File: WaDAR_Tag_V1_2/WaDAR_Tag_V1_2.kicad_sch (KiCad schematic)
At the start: 11 parts, among them J1 SMA-J-P-H-RA-TH1, U1 SiT1569

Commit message: added footprint for SiT1549
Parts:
- U1: footprint (none) -> Library:SiT1569
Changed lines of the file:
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@@
 			)
 		)
-		(property "Footprint" ""
+		(property "Footprint" "Library:SiT1569"
 			(at 67.31 81.28 0)
 			(effects

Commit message: PCB
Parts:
- removed TP1: VCC, JLab_FP:EpicTestPointV1, symbol Connector:TestPoint
- removed TP2: GND, JLab_FP:EpicTestPointV1, symbol Connector:TestPoint
- removed TP3: CLK_OUT, JLab_FP:EpicTestPointV1, symbol Connector:TestPoint

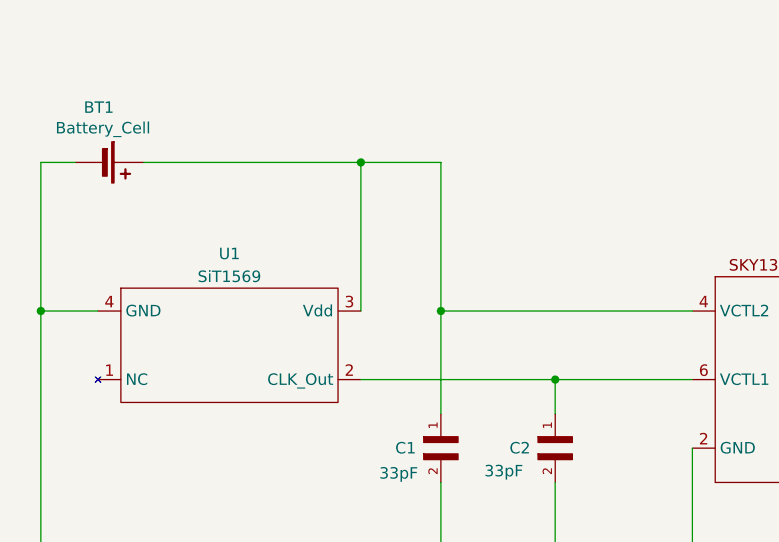
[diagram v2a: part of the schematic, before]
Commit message: added test points, made PCB double sided
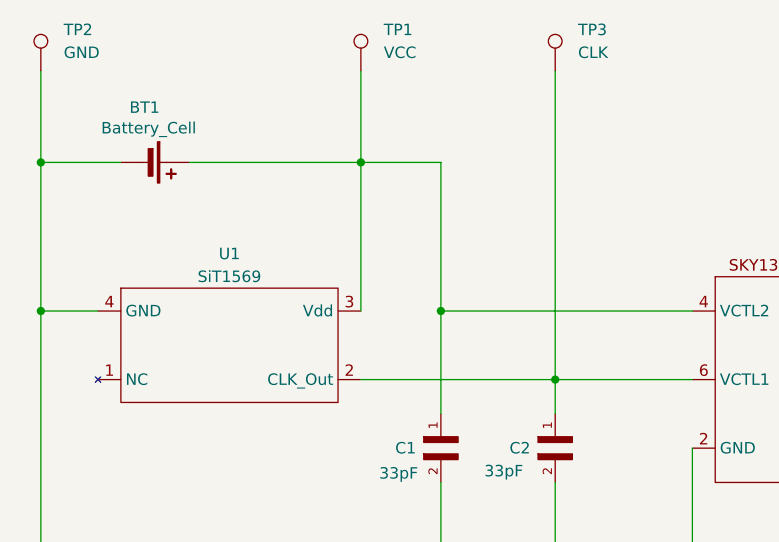
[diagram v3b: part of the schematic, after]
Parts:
- added TP1: VCC, TestPoint:TestPoint_Pad_D1.0mm, symbol Connector:TestPoint
- added TP2: GND, TestPoint:TestPoint_Pad_D1.0mm, symbol Connector:TestPoint
- added TP3: CLK, TestPoint:TestPoint_Pad_D1.0mm, symbol Connector:TestPoint
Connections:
- net GND: now also TP2.1
- net at BT1.1 (+), C1.1, U1.3 (Vdd)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: now also TP1.1
- net at C2.1, U1.2 (CLK_Out), U2.6 (VCTL1): now also TP3.1
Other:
- moved on the sheet: BT1

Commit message: updated datasheets
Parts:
- BT1: value Battery_Cell -> 1060
- C1, C2, C4: symbol GJM1555C1H330JB01D:GJM1555C1H330JB01D -> Device:C
- C3: symbol CBR04C101J3GAC:CBR04C101J3GAC -> Device:C
- U1: value SiT1569 -> SIT1569AC-J3-30E-0000.080000
- U2: value ~ -> SKY13351-378LF; footprint JLab_FP:SKY13351_FP -> Library:SKY13351_FP

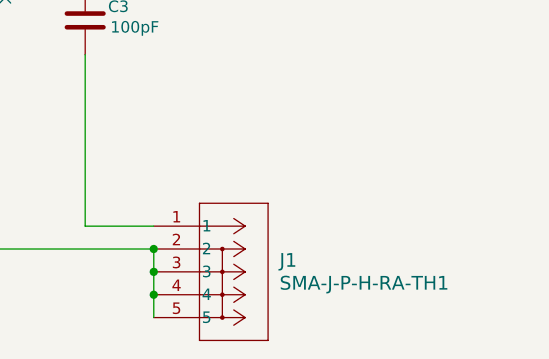
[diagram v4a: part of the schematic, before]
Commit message: added new RF junction
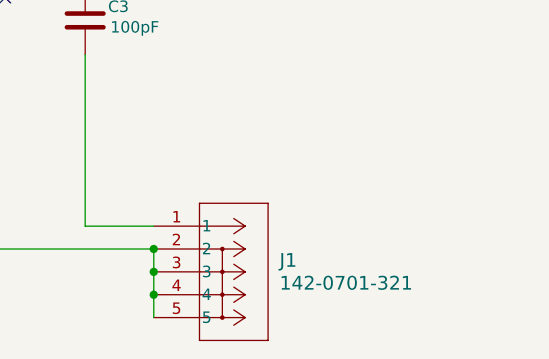
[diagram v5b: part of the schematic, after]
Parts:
- J1: value SMA-J-P-H-RA-TH1 -> 142-0701-321
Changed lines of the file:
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@@
 			)
 		)
-		(property "Value" "SMA-J-P-H-RA-TH1"
+		(property "Value" "142-0701-321"
 			(at 172.72 116.84 0)
 			(effects
@@
 			)
 		)
-		(property "Datasheet" "SMA-J-P-H-RA-TH1"
+		(property "Datasheet" "https://secure-web.cisco.com/1DZ9VzbYAXZ-R-LPek44dWAY5tpyuDxEmXSDugOLt9HCVcz2LxcBg_oyr93yuw77llLCRc9d3T34vo-pjBK-s3IkY3R66W-ncmQ0YOM9IQMUK1O7wZMPkewxqXqTqhK5-2u-29hxEuVjo2LqNmdOEcCusiwmr3znwXKvoiuOikGmvCtdp23G3hZo508RFRhTmv9uOTL0b0hJ-cT9kvkwjuFS8DTf5pSmEP"
 			(at 158.75 110.49 0)
 			(effects
@@
 			)
 		)
-		(property "Description" ""
+		(property "Description" "CONN SMA JACK R/A 50 OHM PCB"
 			(at 158.75 110.49 0)
 			(effects

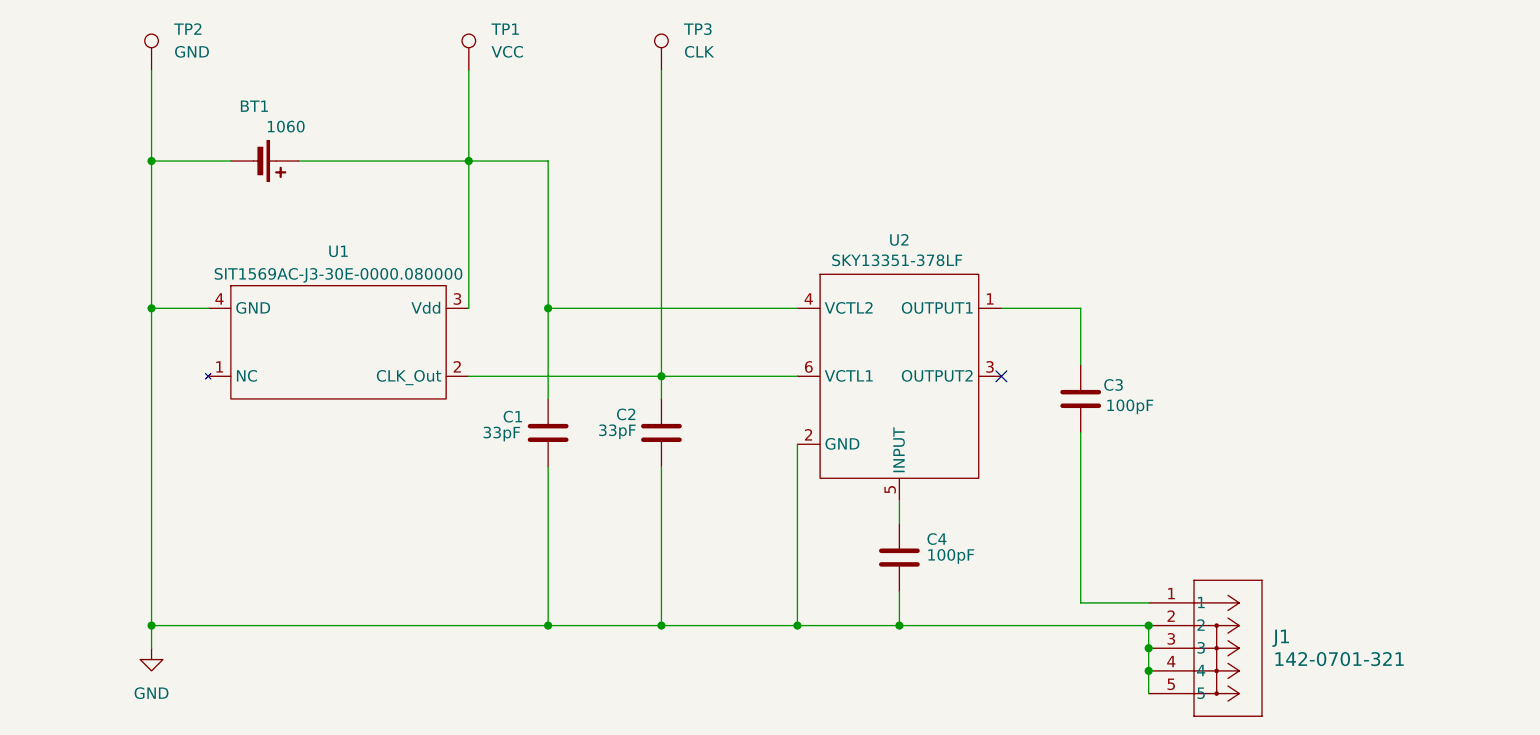
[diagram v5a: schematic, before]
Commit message: updated capacitors and added mounting holes
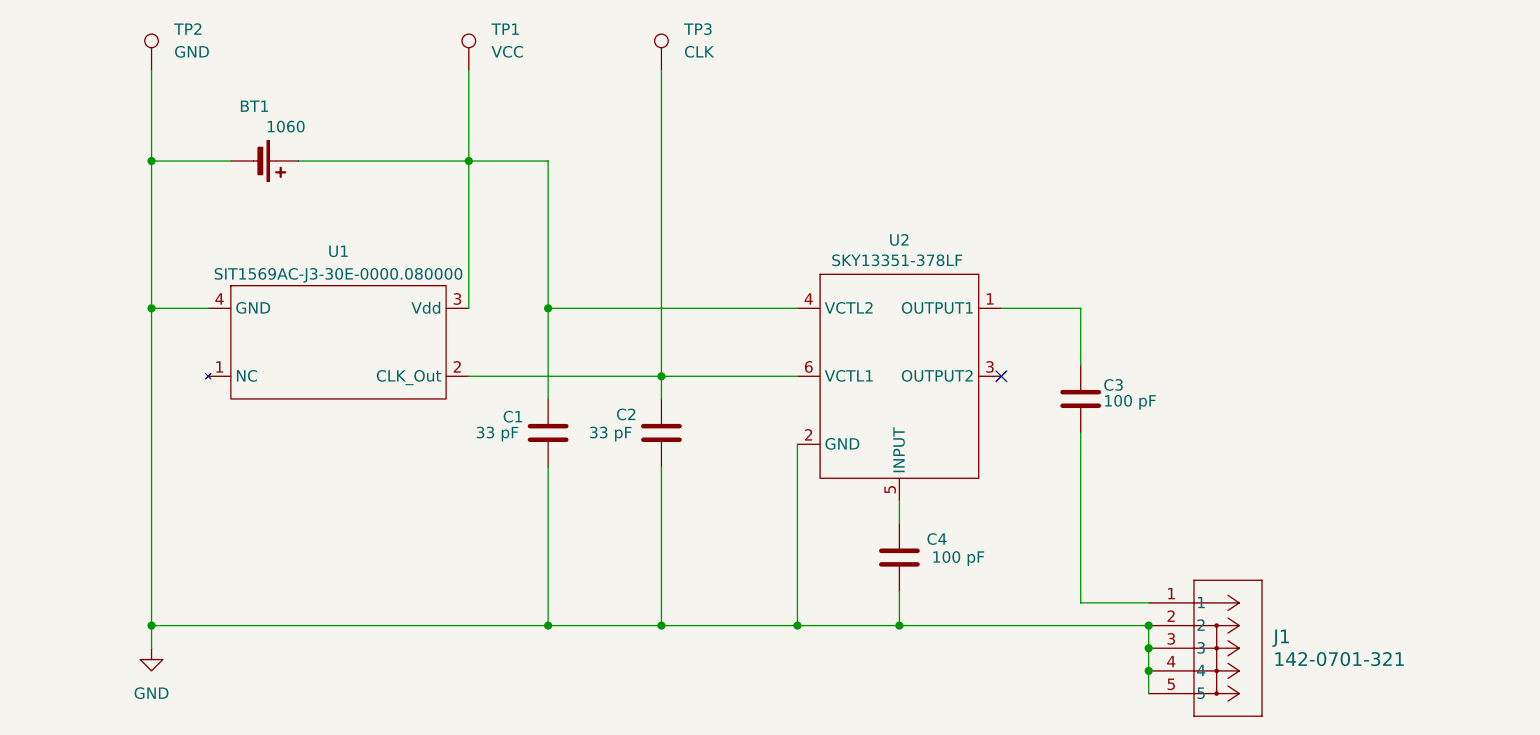
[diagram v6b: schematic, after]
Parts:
- C1, C2: value 33pF -> CAP CER 33PF 0402; Capacitance (none) -> 33 pF
- C3: value 100pF -> CAP CER 100PF 0805; Capacitance (none) -> 100 pF
- C4: value 100pF -> CAP CER 100PF 0402; Capacitance (none) -> 100 pF
- TP1, TP2, TP3: now left out of the parts list
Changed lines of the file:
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@@
 		(unit 1)
 		(exclude_from_sim no)
-		(in_bom yes)
+		(in_bom no)
 		(on_board yes)
 		(dnp no)
@@
 			)
 		)
-		(property "Value" "100pF"
+		(property "Value" "CAP CER 100PF 0805"
 			(at 153.924 88.392 0)
 			(effects
@@
 				)
 				(justify left)
+				(hide yes)
 			)
 		)
@@
 			)
 		)
+		(property "Capacitance" "100 pF"
+			(at 153.67 87.884 0)
+			(effects
+				(font
+					(size 1.27 1.27)
+				)
+				(justify left)
+			)
+		)
 		(pin "1"
 		)
@@
 			)
 		)
-		(property "Value" "100pF"
+		(property "Value" "CAP CER 100PF 0402"
 			(at 133.858 105.156 0)
 			(effects
@@
 				)
 				(justify left)
+				(hide yes)
 			)
 		)
@@
 			)
 		)
+		(property "Capacitance" "100 pF"
+			(at 137.414 104.648 0)
+			(effects
+				(font
+					(size 1.27 1.27)
+				)
+				(justify top)
+			)
+		)
 		(pin "1"
 		)
@@
 		(unit 1)
 		(exclude_from_sim no)
-		(in_bom yes)
+		(in_bom no)
 		(on_board yes)
 		(dnp no)
@@
 			)
 		)
-		(property "Value" "33pF"
+		(property "Value" "CAP CER 33PF 0402"
 			(at 97.028 91.186 0)
 			(effects
@@
 				)
 				(justify left)
+				(hide yes)
 			)
 		)
@@
 			)
 		)
+		(property "Capacitance" "33 pF"
+			(at 96.012 91.44 0)
+			(effects
+				(font
+					(size 1.27 1.27)
+				)
+				(justify left)
+			)
+		)
 		(pin "1"
 		)
@@
 		(unit 1)
 		(exclude_from_sim no)
-		(in_bom yes)
+		(in_bom no)
 		(on_board yes)
 		(dnp no)
@@
 			)
 		)
-		(property "Value" "33pF"
+		(property "Value" "CAP CER 33PF 0402"
 			(at 84.074 91.44 0)
 			(effects
@@
 				)
 				(justify left)
+				(hide yes)
 			)
 		)
@@
 			)
 		)
+		(property "Capacitance" "33 pF"
+			(at 83.312 91.44 0)
+			(effects
+				(font
+					(size 1.27 1.27)
+				)
+				(justify left)
+			)
+		)

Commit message: V_2 off to assembly
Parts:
- added TP4: GND, TestPoint:TestPoint_Pad_D1.0mm, symbol Connector:TestPoint
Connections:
- net GND: now also TP4.1
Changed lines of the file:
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@@
+	(wire
+		(pts
+			(xy 39.37 60.96) (xy 46.99 60.96)
+		)
+		(stroke
+			(width 0)
+			(type default)
+		)
+	)
 	(wire
 		(pts
@@
 		(pts
 			(xy 151.13 77.47) (xy 142.24 77.47)
+		)
+		(stroke
+			(width 0)
+			(type default)
+		)
+	)
+	(wire
+		(pts
+			(xy 39.37 50.8) (xy 39.37 60.96)
 		)
 		(stroke
@@
 					(unit 1)
 				)
+			)
+		)
+	)
+	(symbol
+		(lib_id "Connector:TestPoint")
+		(at 39.37 50.8 0)
+		(mirror y)
+		(unit 1)
+		(exclude_from_sim no)
+		(in_bom no)
+		(on_board yes)
+		(dnp no)
+		(property "Reference" "TP4"
+			(at 36.83 46.2279 0)
+			(effects
+				(font
+					(size 1.27 1.27)
+				)
+				(justify left)
+			)
+		)
+		(property "Value" "GND"
+			(at 36.83 48.7679 0)
+			(effects
+				(font
+					(size 1.27 1.27)
+				)
+				(justify left)
+			)
+		)
+		(property "Footprint" "TestPoint:TestPoint_Pad_D1.0mm"
+			(at 34.29 50.8 0)
+			(effects
+				(font
+					(size 1.27 1.27)
+				)
+				(hide yes)
+			)
+		)
+		(property "Datasheet" "~"
+			(at 34.29 50.8 0)
+			(effects
+				(font
+					(size 1.27 1.27)
+				)
+				(hide yes)
+			)
+		)
+		(property "Description" "test point"
+			(at 39.37 50.8 0)
+			(effects
+				(font
+					(size 1.27 1.27)
+				)
+				(hide yes)
+			)
+		)
+		(pin "1"
+		)
+		(instances
+			(project "WaDAR_Tag_V1_2"
+				(path "/1b480a55-1292-4321-8fce-0463cf94490c"
+					(reference "TP4")
+					(unit 1)
+				)
